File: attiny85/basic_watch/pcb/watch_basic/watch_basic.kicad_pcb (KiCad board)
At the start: 2 copper layers, 39.9 x 41.8 mm, 22 parts, among them J3 Programmer, P1 JST_LIPO, U2 MCP73831-2-OT

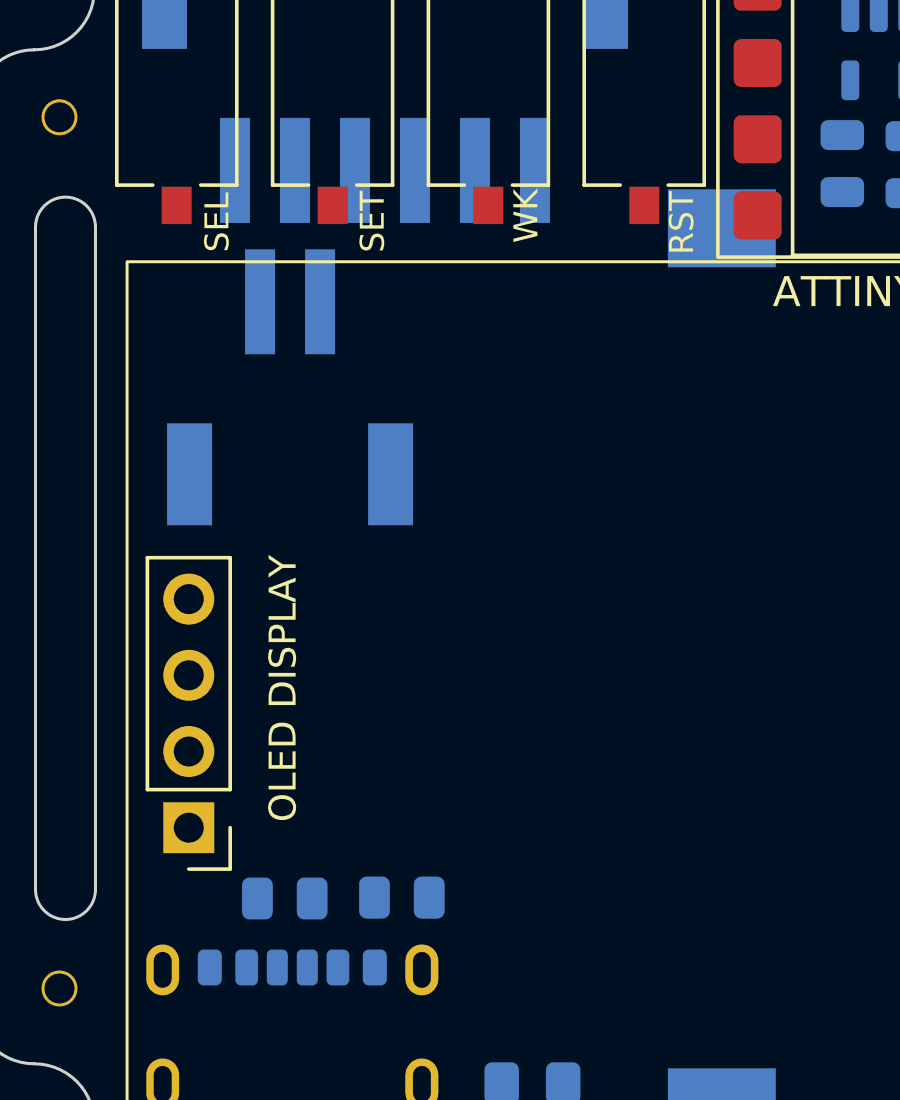
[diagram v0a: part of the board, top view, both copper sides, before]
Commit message: split by basic and charger versions
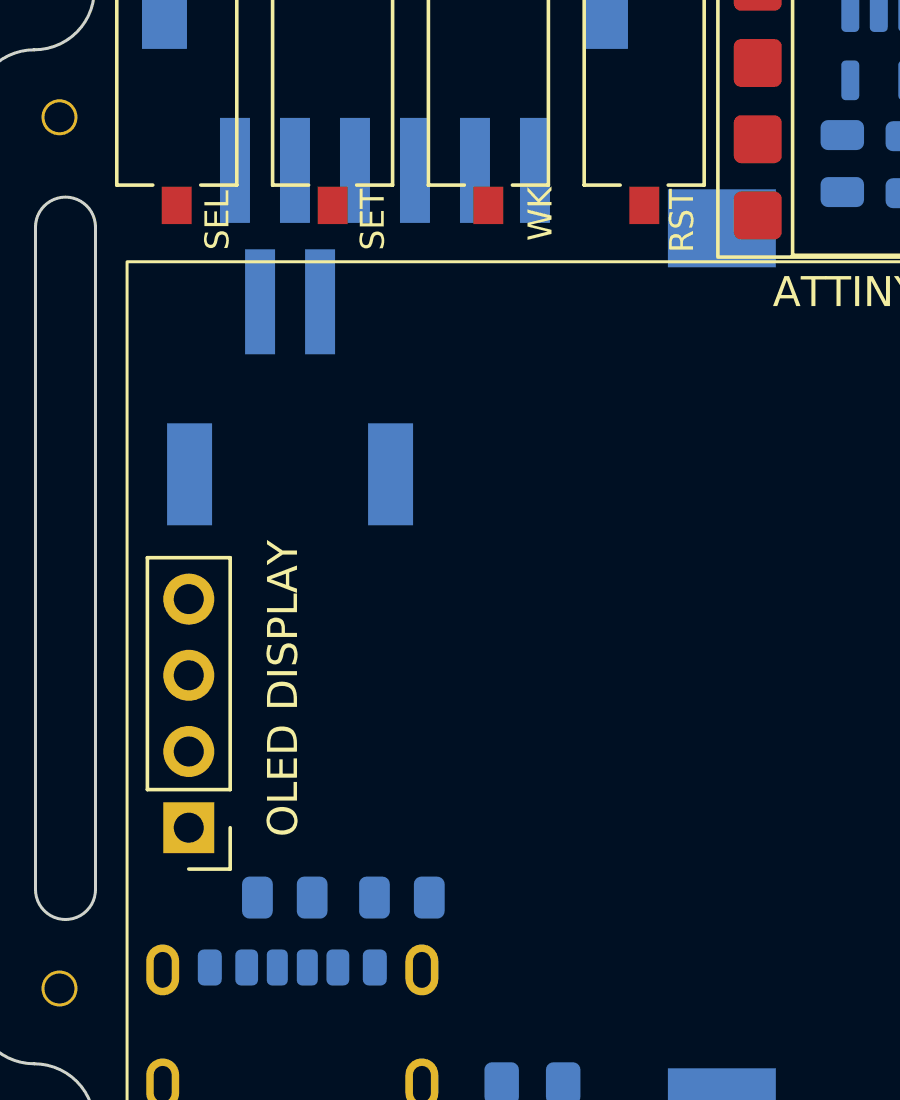
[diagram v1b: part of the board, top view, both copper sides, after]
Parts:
- renumbered J3 to JPROG, LED1 to LED
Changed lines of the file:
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@@
 			(effects
 				(font
-					(size 0.9 0.9)
+					(size 1 1)
 					(thickness 0.15)
 				)
@@
 		(tags "switch tactile SPST 1P1T straight NO SMTR C&K")
 		(property "Reference" "RST"
-			(at -4.46 1.26 90)
+			(at -4.389998 1.26 90)
 			(unlocked yes)
 			(layer "F.SilkS")
@@
 				(font
 					(size 0.8 0.8)
-					(thickness 0.15)
+					(thickness 0.1)
 				)
 			)
@@
 		(tags "switch tactile SPST 1P1T straight NO SMTR C&K")
 		(property "Reference" "SEL"
-			(at -4.440952 1.35 90)
+			(at -4.37095 1.35 90)
 			(unlocked yes)
 			(layer "F.SilkS")
@@
 				(font
 					(size 0.8 0.8)
-					(thickness 0.15)
+					(thickness 0.1)
 				)
 			)
@@
 		(tags "switch tactile SPST 1P1T straight NO SMTR C&K")
 		(property "Reference" "SET"
-			(at -4.421905 1.336667 90)
+			(at -4.351903 1.336667 90)
 			(unlocked yes)
 			(layer "F.SilkS")
@@
 				(font
 					(size 0.8 0.8)
-					(thickness 0.15)
+					(thickness 0.1)
 				)
 			)
@@
 		(tags "switch tactile SPST 1P1T straight NO SMTR C&K")
 		(property "Reference" "WK"
-			(at -4.231428 1.263333 90)
+			(at -4.161426 1.733333 90)
 			(unlocked yes)
 			(layer "F.SilkS")
@@
 				(font
 					(size 0.8 0.8)
-					(thickness 0.15)
+					(thickness 0.1)
 				)
 			)
@@
 		(tags "capacitor")
 		(property "Reference" "C1"
-			(at -0.261252 -1.543756 90)
+			(at -2.698004 0.870745 90)
 			(layer "B.SilkS")
 			(effects
@@
 		(tags "CR2032 BR2032 BatteryHolder Battery")
 		(property "Reference" "BT1"
-			(at -14.125 5.3 90)
+			(at 13.01 -4.87 90)
 			(layer "B.SilkS")
 			(effects
@@
 		(layer "B.Cu")
 		(at 139.65 73.61)
-		(property "Reference" "J3"
-			(at 9.78 -6.75 180)
+		(property "Reference" "JPROG"
+			(at 9.67 -3.39 270)
 			(layer "B.SilkS")
 			(effects
@@
 			(effects
 				(font
-					(size 0.9 0.9)
+					(size 1 1)
 					(thickness 0.15)
 				)
@@
 		(tags "resistor")
 		(property "Reference" "R4"
-			(at 2.595119 0.2381 90)
+			(at 2.595119 0.189728 90)
 			(layer "B.SilkS")
 			(effects
 				(font
-					(size 0.9 0.9)
+					(size 1 1)
 					(thickness 0.15)
 				)
@@
 			(effects
 				(font
-					(size 1.001079 1.001079)
+					(size 1 1)
 					(thickness 0.15)
 				)
@@
 		(tags "capacitor")
 		(property "Reference" "C2"
-			(at 2.048209 -0.110789 90)
+			(at 2.66 -0.624501 90)
 			(layer "B.SilkS")
 			(effects
@@
 	(footprint "Resistor_SMD:R_0805_2012Metric"
 		(layer "B.Cu")
-		(at 136.31 97.88 180)
+		(at 136.31 97.85 180)
 		(descr "Resistor SMD 0805 (2012 Metric), square (rectangular) end terminal, IPC-7351 nominal, (Body size source: IPC-SM-782 page 72, https://www.pcb-3d.com/wordpress/wp-content/uploads/ipc-sm-782a_amendment_1_and_2.pdf), generated with kicad-footprint-generator")
 		(tags "resistor")
@@
 		(tags "resistor")
 		(property "Reference" "R3"
-			(at -0.04074 1.49074 90)
+			(at -2.631791 0.329969 90)
 			(layer "B.SilkS")
 			(effects
 				(font
-					(size 0.9 0.9)
+					(size 1 1)
 					(thickness 0.15)
 				)
@@
 		(tags "SOT TO_SOT_SMD")
 		(property "Reference" "U2"
-			(at 2.993918 -2.070278 90)
+			(at 0.139291 2.84 90)
 			(layer "B.SilkS")
-			(hide yes)
 			(effects
 				(font
-					(size 0.8 0.8)
+					(size 1 1)
 					(thickness 0.15)
 				)
@@
 		)
 		(fp_text user "${REFERENCE}"
-			(at 0 0 180)
+			(at 0 0 0)
 			(layer "B.Fab")
 			(effects
@@
 		(descr "LED SMD 0805 (2012 Metric), square (rectangular) end terminal, IPC-7351 nominal, (Body size source: https://docs.google.com/spreadsheets/d/1BsfQQcO9C6DZCsRaXUlFlo91Tg2WpOkGARC1WS5S8t0/edit?usp=sharing), generated with kicad-footprint-generator")
 		(tags "LED handsolder")
-		(property "Reference" "LED1"
-			(at -5.656051 0.959229 180)
+		(property "Reference" "LED"
+			(at 0.105 1.77 180)
 			(layer "B.SilkS")
-			(hide yes)
 			(effects
 				(font
